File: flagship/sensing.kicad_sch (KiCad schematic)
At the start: 0 parts

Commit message: flagship: schematic skeleton across all seven sheets
Candidate ICs placed with cross-sheet nets as global labels and a design note per sheet
citing the record: LTC4364IS-2 input protection with INA228 Kelvin shunt and mirrored bulk;
TPS48111 back-to-back motor switch with pre-charge, MOTOR_EN pulldown, INA ALERT hardware
cut; TLV1805 + TLV431 self-acting regen clamp, 2x TO-263, external connector and
parallel/replace jumper; 3x TPS54560B bucks (12/5/3.3 V); Stamp-P4 with fixed pins only
(GPIO assignment follows layout, per ruling); THVD1450 RS485, 74AHCT125 quadrature, drive
status inputs; INA228, thermistor and fan headers. Connectors are generic placeholders.

SPEC.md: rulings for no RP2350 (P4 LP-core emits quadrature) and passive sizes.
Libraries normalized to ASCII (LCSC Chinese manufacturer names, en-dash pin name) after
they broke the MCP server's Windows-codepage reads.

ERC: 109 unconnected pins (detailing), 62 pin-type warnings (LCSC symbols ship
unspecified pin types), 13 one-sided labels (GPIO pending layout); 0 dangling.

Co-Authored-By: Claude Opus 5.5 (1M context) <noreply@anthropic.com>
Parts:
- added C13, C14: 0.1u, Capacitor_SMD:C_0805_2012Metric, symbol Device:C
- added J6: THERMISTOR, symbol Connector_Generic:Conn_01x02
- added J7: FAN_4PIN, symbol Connector_Generic:Conn_01x04
- added JP2: FAN_V_12V|5V, symbol Jumper:SolderJumper_3_Open
- added R24, R25: 4.7k, Resistor_SMD:R_0805_2012Metric, symbol Device:R
- added R26, R28: 10k, Resistor_SMD:R_0805_2012Metric, symbol Device:R
- added R27, R29: 1k, Resistor_SMD:R_0805_2012Metric, symbol Device:R
- added U11: INA228, flagship:VSSOP-10_L3.0-W3.0-P0.50-LS4.9-BL, symbol flagship:INA228AIDGSR
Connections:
- new net +12V: JP2.1 (A)
- new net +3V3: C13.1, R24.1, R25.1, R26.1, R28.1, U11.6 (VS)
- new net +5V: JP2.3 (B)
- new net +BUS: U11.8 (VBUS)
- new net FAN_PWM: J7.4 (Pin_4)
- new net FAN_TACH: R29.2
- new net FAN_TACH_IN: J7.3 (Pin_3), R28.2, R29.1
- new net FAN_V: J7.2 (Pin_2), JP2.2 (C)
- new net GND: C13.2, C14.2, J6.2 (Pin_2), J7.1 (Pin_1), U11.1 (A1), U11.2 (A0), U11.7 (GND)
- new net I2C_SCL: R25.2, U11.5 (SCL)
- new net I2C_SDA: R24.2, U11.4 (SDA)
- new net INA_ALERT_N: U11.3 (ALERT)
- new net INA_SENSE_N: U11.9 (IN-)
- new net INA_SENSE_P: U11.10 (IN+)
- new net THERM: C14.1, R27.2
- new net THERM_IN: J6.1 (Pin_1), R26.2, R27.1
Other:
- note added: "SENSING (record sections 10, 12). U11 INA228 across R2 on the Input sheet via Kelvin taps INA_SENSE_P/N: route as a tight pair, INA beside the shunt, quiet ground, far from switch nodes. 1 mOhm: 10 mV at 10 A, inside the +-163.84 mV range; die temperature = board temperature (the thermal witness per the heatsink ruling). ALERT (open drain) = INA_ALERT_N: also the motor switch EN/UVLO, so over-cur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"

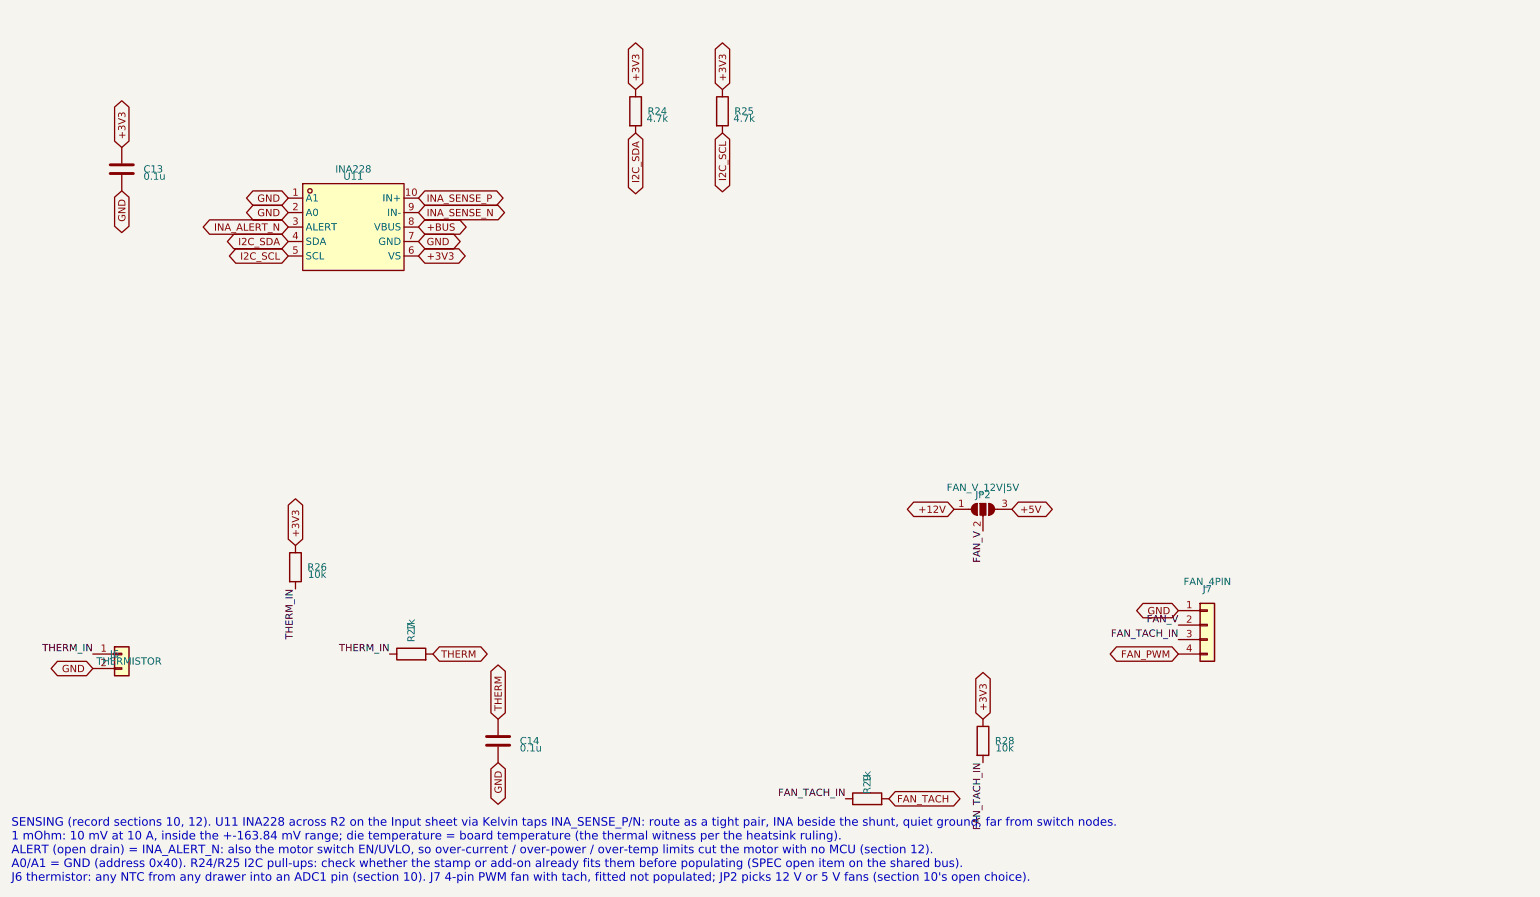
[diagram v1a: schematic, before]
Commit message: flagship: rails detailed per the TPS54560B datasheet; logic power moved to the stamp's own rails
Rails: three identical 400 kHz columns (A3 sheet), 4 A each, VIN 20-48 V, UVLO 20/17 V,
values from the datasheet design procedure (inductor, derated ceramic output, FB, type-II
comp, B560C catch diode, 4x 2.2u/100V input). Worst on-time 205 ns vs 135 ns minimum.
Logic power (operator): +5V_SYS = stamp pad 39 (VIN/USB OR) feeds the 74AHCT125, drive
485_5V and status LED, so USB alone emits quadrature; +3V3_SYS = stamp pad 28 feeds the
INA228, THVD1450 and all pull-ups. 3.3 V buck is accessory-only (+3V3_ACC). Netlist checked:
the five power domains are separate. SPEC rulings recorded.

Co-Authored-By: Claude Opus 5.5 (1M context) <noreply@anthropic.com>
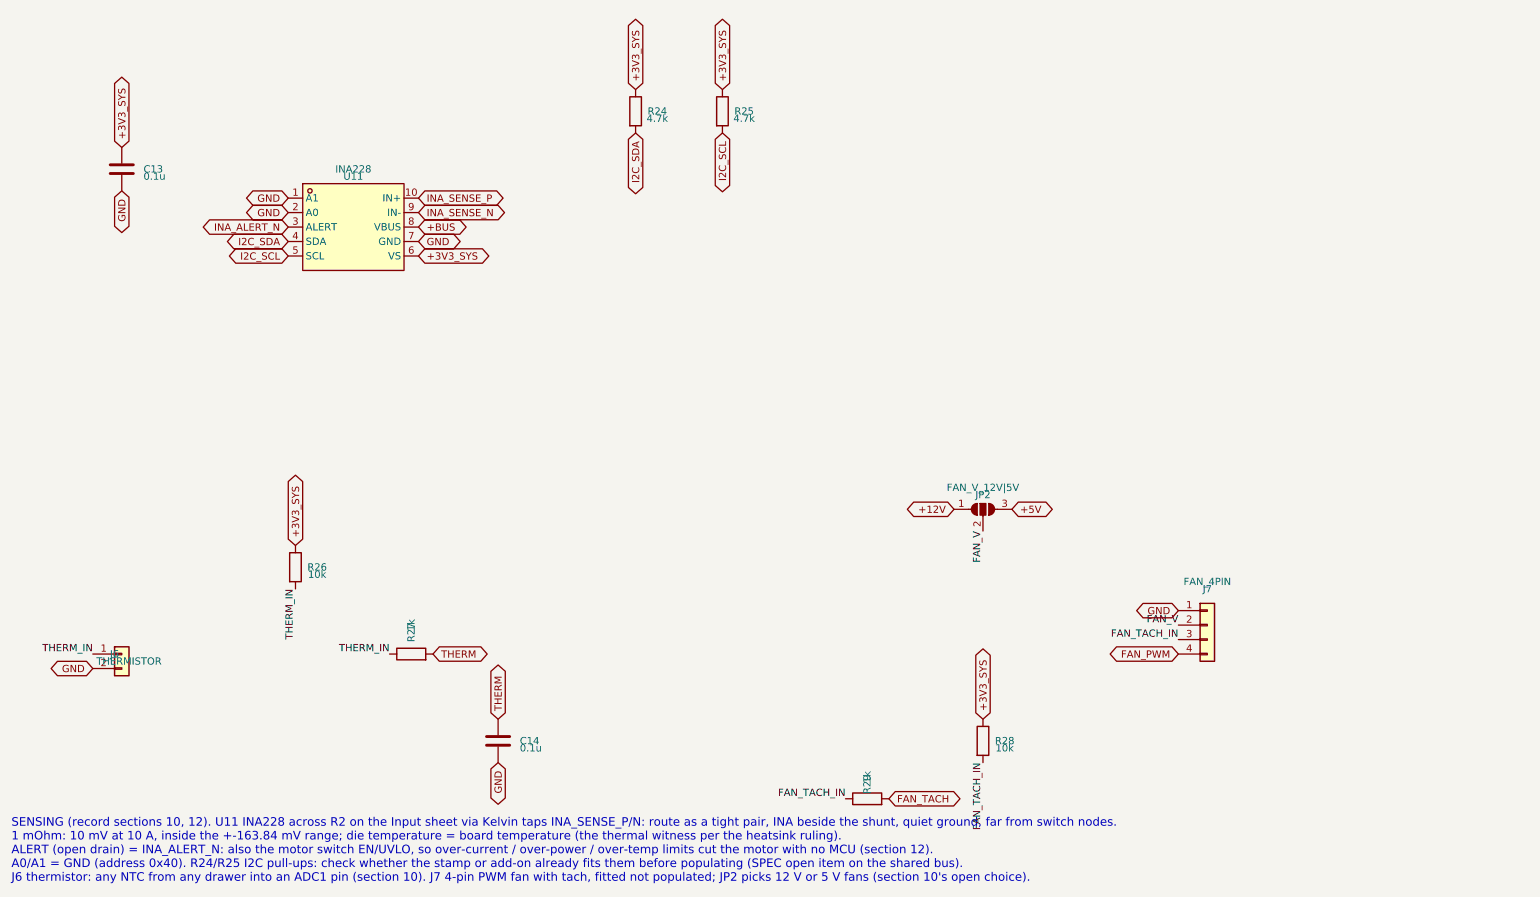
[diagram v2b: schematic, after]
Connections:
- net +3V3 renamed +3V3_SYS
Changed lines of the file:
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@@
 		)
 	)
-	(global_label "+3V3"
+	(global_label "+3V3_SYS"
 		(shape bidirectional)
 		(at 39.37 55.88 90)
@@
 		)
 	)
-	(global_label "+3V3"
+	(global_label "+3V3_SYS"
 		(shape bidirectional)
 		(at 144.78 45.72 90)
@@
 		)
 	)
-	(global_label "+3V3"
+	(global_label "+3V3_SYS"
 		(shape bidirectional)
 		(at 91.44 74.93 0)
@@
 		)
 	)
-	(global_label "+3V3"
+	(global_label "+3V3_SYS"
 		(shape bidirectional)
 		(at 129.54 45.72 90)
@@
 		)
 	)
-	(global_label "+3V3"
+	(global_label "+3V3_SYS"
 		(shape bidirectional)
 		(at 69.85 125.73 90)
@@
 		)
 	)
-	(global_label "+3V3"
+	(global_label "+3V3_SYS"
 		(shape bidirectional)
 		(at 190.5 156.21 90)
